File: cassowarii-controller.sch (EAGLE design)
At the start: 22 parts, among them J1 2-PIN_2MM-H, J2 2-PIN_2MM-H, J3 AVR_SPI_PROG_3X2PTH, J4 Power, U1 ATTiny85, U2 AZ1117IH

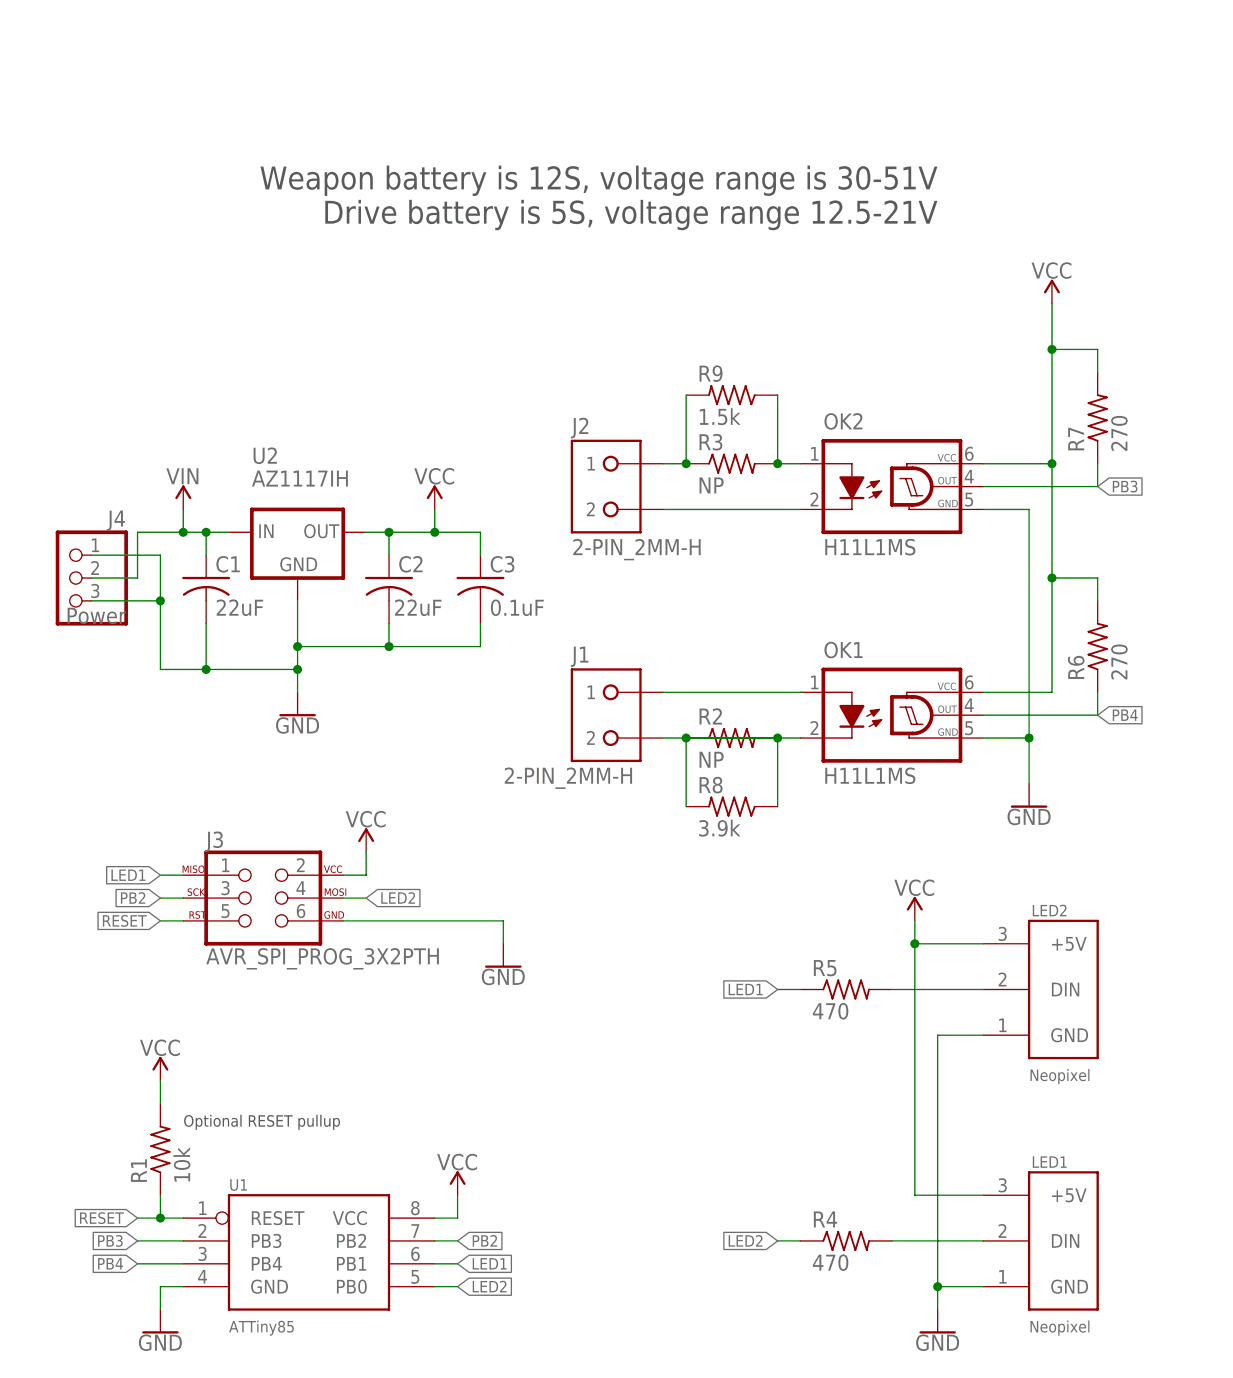
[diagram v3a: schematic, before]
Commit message: Remove regulator
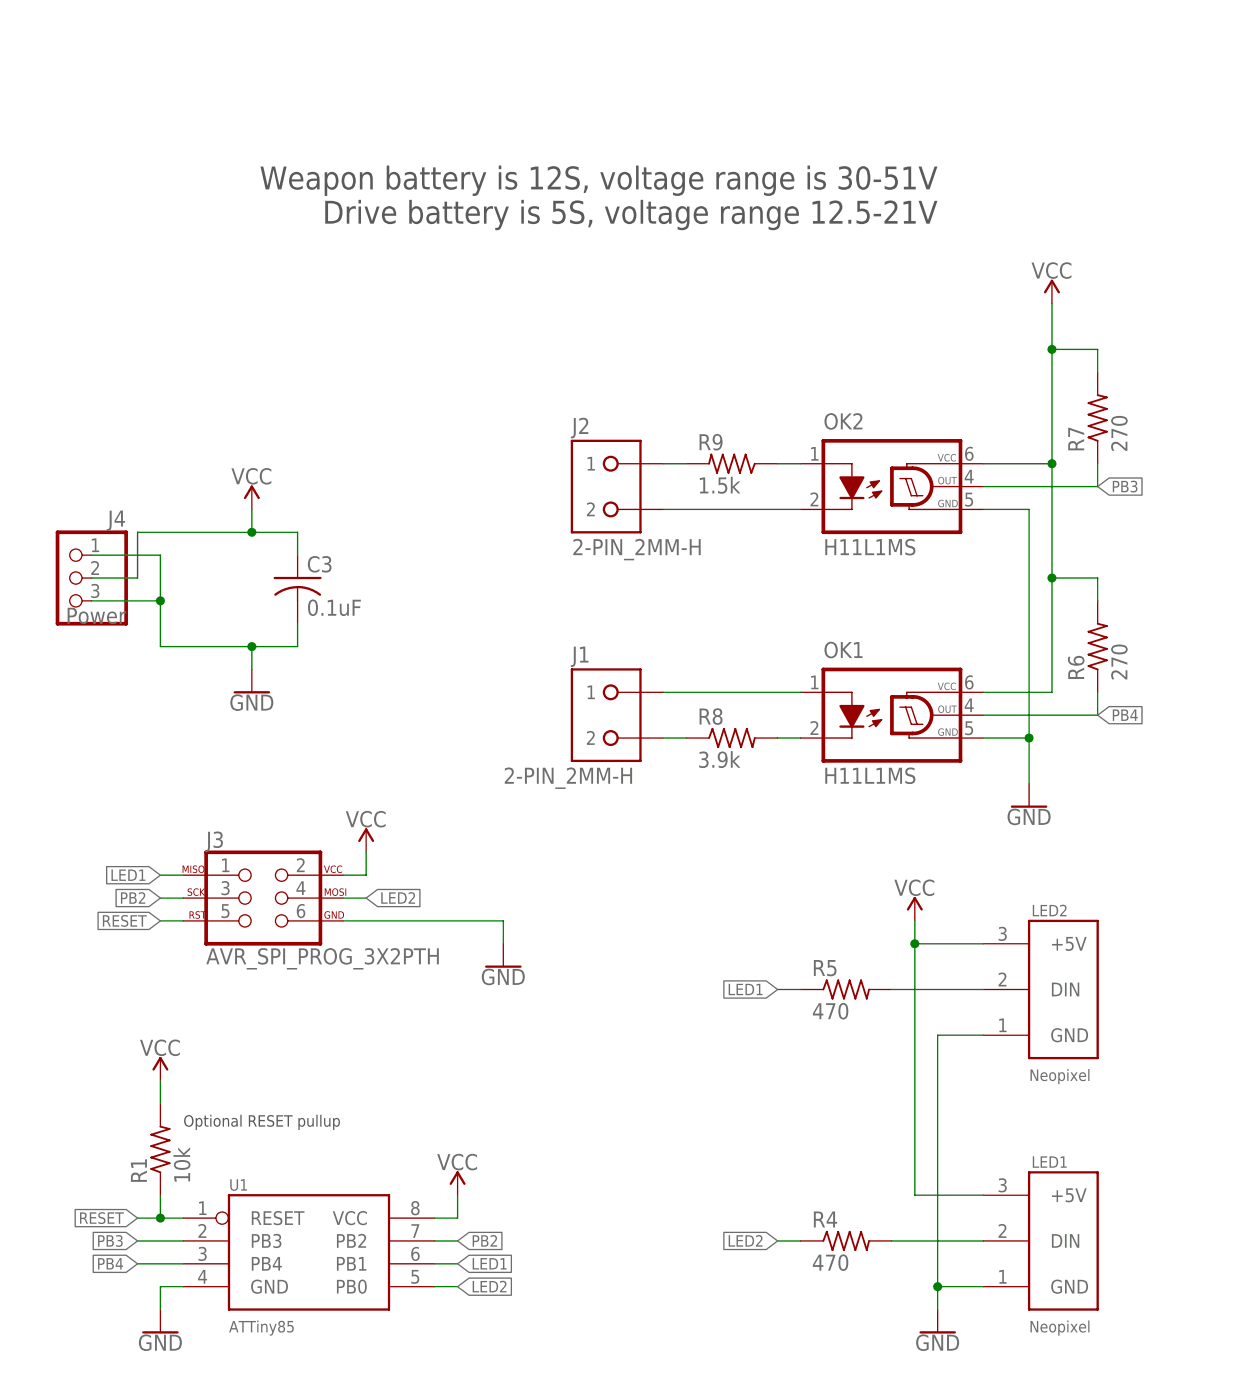
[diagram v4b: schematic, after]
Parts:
- removed C1, C2: 22uF, resistor:C-USC0805
- removed R2, R3: NP, resistor:R-US_R0805
- removed U2: AZ1117IH, JoshCustom:AZ1117IH
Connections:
- removed net VIN: C1.1, J4.2, U2.IN
- net GND: no longer C1.2, C2.2, U2.GND
- net N$10: no longer R3.2
- net N$3: no longer R3.1
- net N$4: no longer R2.2
- net N$5: no longer R2.1
- net VCC: now also J4.2; no longer C2.1, U2.OUT
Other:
- moved on the sheet: C3, R8, R9

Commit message: Replace optoisolator
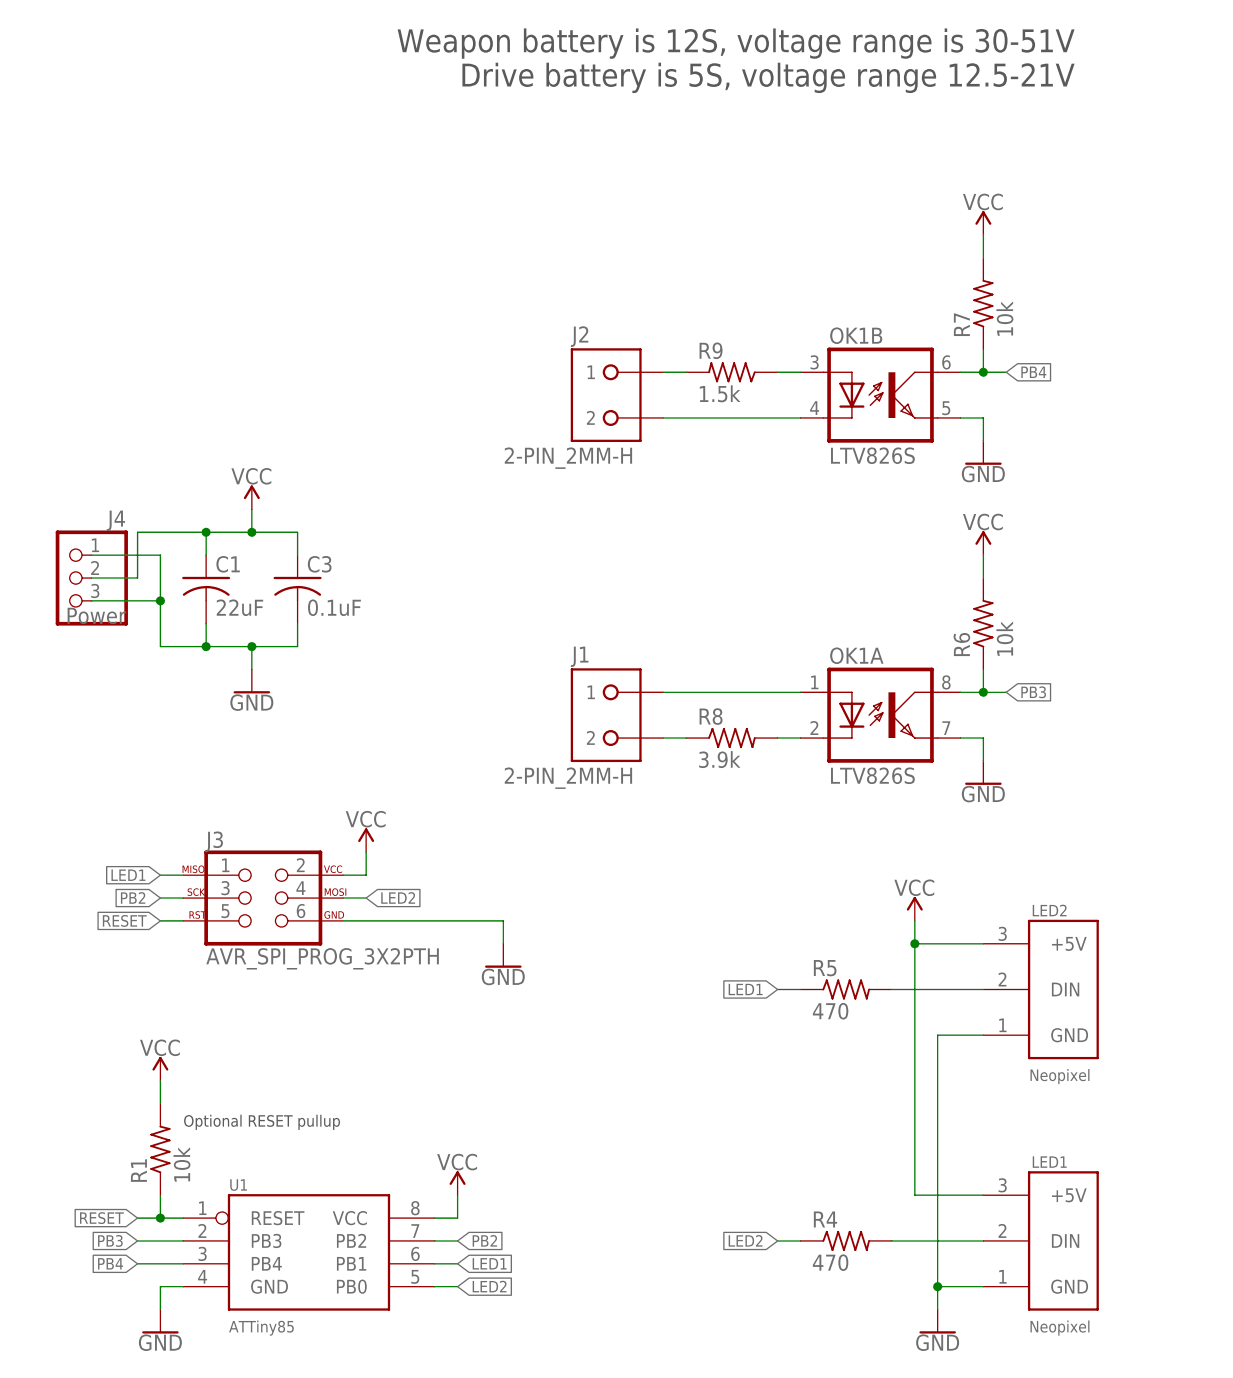
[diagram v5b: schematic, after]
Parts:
- removed OK2: H11L1MS, optocoupler:H11L1MS
- added C1: 22uF, resistor:C-USC0805
- OK1: value H11L1MS -> LTV826S; device optocoupler:H11L1MS -> optocoupler:LTV826S
- R6, R7: value 270 -> 10k
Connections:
- removed net N$10: OK2.A, R9.1
- new net N$8: OK1A.C, R8.2
- net GND: now also C1.2, OK1A.EMIT, OK1B.EMIT; no longer OK1.GND, OK2.GND
- net N$5: now also OK1B.A, R9.1; no longer OK1.C, R8.2
- net N$6: now also OK1B.C; no longer OK2.C
- net N$7: now also OK1A.A; no longer OK1.A
- net PB3: now also OK1A.COL, R6.1; no longer OK2.OUT, R7.1
- net PB4: now also OK1B.COL, R7.1; no longer OK1.OUT, R6.1
- net VCC: now also C1.1; no longer OK1.VCC, OK2.VCC
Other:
- moved on the sheet: J2, R6, R7, R9
